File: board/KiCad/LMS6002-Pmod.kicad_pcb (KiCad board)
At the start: 2 copper layers, 76.2 x 48.8 mm, 58 parts, among them CON1 BARREL_JACK, J1 FX10B_80S_8, J2 Pinheader_1x6_TH, J3 SELECT_DIV, P1 PMOD_2x6, P2 PMOD_2x6, P3 Myriad_Mount_Hole, P4 Myriad_Mount_Hole, Q1 Q_PMOS_GSD, SW1 ICE_RESET, T1 OSHW_Logo, U1 iCE40_1K4K_TQ144, U2 LD6815, U3 LTC1799, U4 N25Q

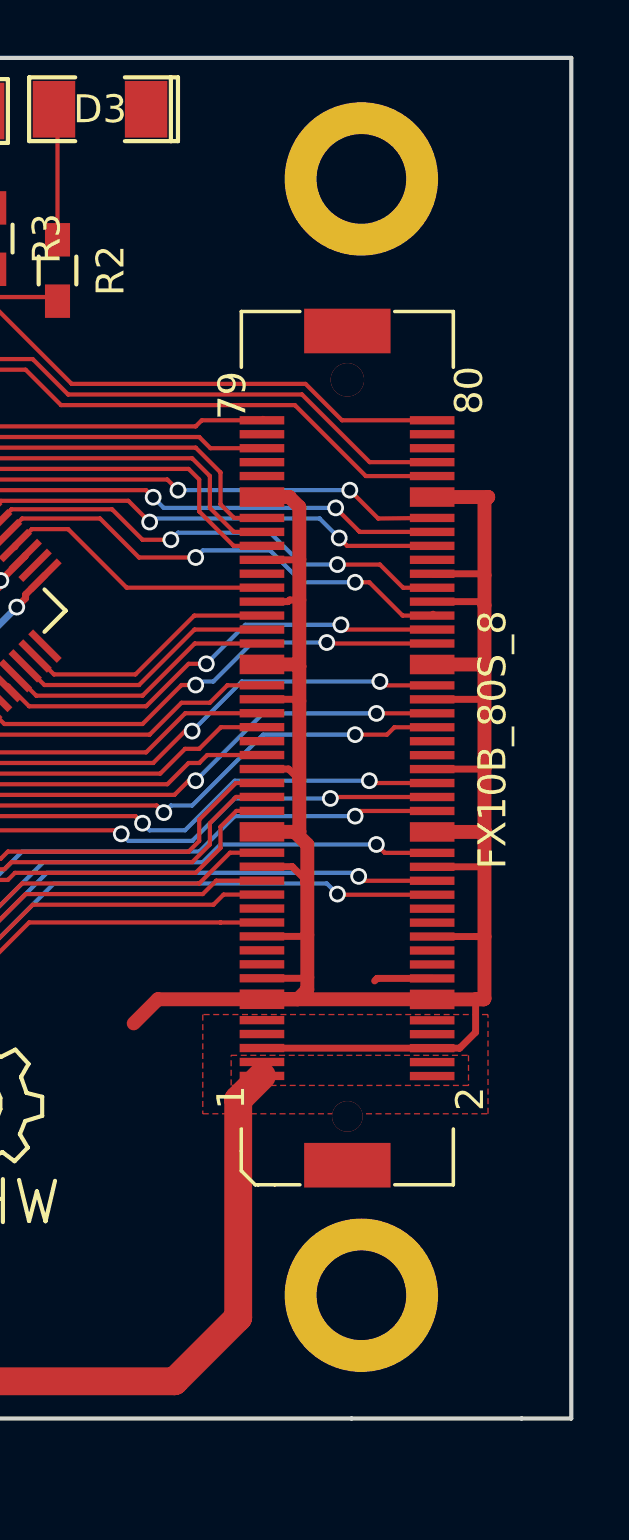
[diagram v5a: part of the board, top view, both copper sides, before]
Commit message: Housekeeping
Structure libraries and put proper licenses to them.
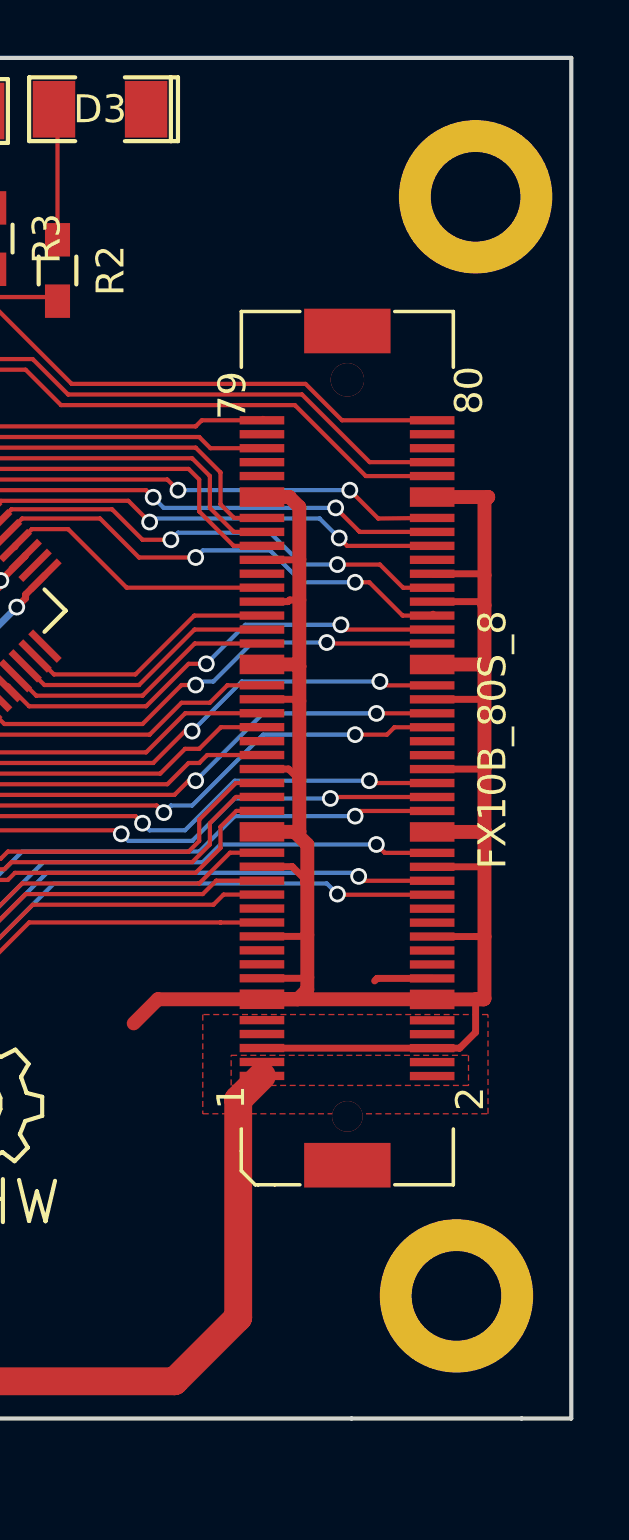
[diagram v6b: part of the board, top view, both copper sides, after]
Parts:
- CON1: footprint Connect:BARREL_JACK -> lms6002-pmod:BARREL_JACK
- D1: footprint pmod:SOD-123F_Handsoldering -> lms6002-pmod:SOD-123F_Handsoldering
- D2: footprint pmod:SOD-123_Handsoldering -> lms6002-pmod:SOD-123_Handsoldering
- J1: footprint pmod:FX10B_80S_8 -> MyriadRF:FX10B_80S_8
- P1: footprint pmod:Pmod -> lms6002-pmod:Pmod
- P2: footprint pmod:Pmod -> lms6002-pmod:Pmod_no_header
- P3, P4: footprint pmod:Myriad_Mount_Hole -> lms6002-pmod:Myriad_Mount_Hole
- SW1: footprint pmod:B3U-1000P_Handsoldering -> lms6002-pmod:B3U-1000P_Handsoldering
- U2: footprint pmod:SOT-753_(TSOP-5)_Handsoldering -> lms6002-pmod:SOT-753_(TSOP-5)_Handsoldering
- U3: footprint pmod:TSOT-23_Handsoldering -> lms6002-pmod:TSOT-23_Handsoldering
- U4: footprint pmod:SOP2-8_Handsoldering -> lms6002-pmod:SOP2-8_Handsoldering
